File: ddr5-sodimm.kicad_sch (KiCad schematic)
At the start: 22 parts, among them J2 BUS_DDR5_SODIMM_AMPHENOL_1016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

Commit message: Connect DDR hierarchical labels. Define and connect JTAG, RGMII, TDMS, UART, and SDIO buses. Reorganize schematic blocks between sheets
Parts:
- removed J2: BUS_DDR5_SODIMM_AMPHENOL_10161033-002RHLF, sodimm-ddr5-tester-footprints:DDR5_AMPHENOL_10161033-002RHLF, symbol sodimm-ddr5-tester:BUS_DDR5_SODIMM_AMPHENOL_10161033-002RHLF
- added C127: C_1u_0402, sodimm-ddr5-tester-footprints:C_0402_1005Metric, symbol sodimm-ddr5-tester:C_1u_0402
- added D9: LED_RGY_0606_APTF1616SURKCGKSYKC, sodimm-ddr5-tester-footprints:LED_RGY_1.6x1.6mm_APTF1616, symbol sodimm-ddr5-tester:LED_RGY_0606_APTF1616SURKCGKSYKC
- added J2: Bus_DDR5_SODIMM_Amphenol_10161033-002RHLF_2xDetec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, antmicro-footprints:Bus_DDR5_SODIMM_Amphenol_10161033-002RHLF, symbol antmicroMemoryConnectorsPCCardSockets:Bus_DDR5_SODIMM_Amphenol_10161033-002RHLF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
- added Q10, Q11, Q9: BSS138PW, sodimm-ddr5-tester-footprints:SC70-3, symbol sodimm-ddr5-tester:BSS138PW
- added R128: R_10k_0402, sodimm-ddr5-tester-footprints:R_0402_1005Metric, symbol sodimm-ddr5-tester:R_10k_0402
- added R61, R62, R63: R_330R_0402, sodimm-ddr5-tester-footprints:R_0402_1005Metric, symbol sodimm-ddr5-tester:R_330R_0402
- added R78: R_4k7_0402, sodimm-ddr5-tester-footprints:R_0402_1005Metric, symbol sodimm-ddr5-tester:R_4k7_0402
- added SW3: SW_KMR211NGLFS_SMD, sodimm-ddr5-tester-footprints:SW_KMR211NGLFS_SMD, symbol sodimm-ddr5-tester:SW_KMR211NGLFS_SMD
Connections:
- net +3V3: now also D9.1 (A), R78.1
- net +5V: now also J2.1 (VIN_BULK), J2.3 (VIN_BULK)
- net A.DQ0: now also J2.11 (DQ0_A)
- net A.DQ1: now also J2.12 (DQ1_A)
- net B.DQ0: now also J2.179 (DQ0_B)
- net B.DQ1: now also J2.180 (DQ1_B)
- net Control.~{ALERT}: now also J2.108 (ALERT_n)
- net GND: now also C127.2, J2.10 (VSS), J2.101 (VSS), J2.104 (VSS), J2.105 (VSS), J2.111 (VSS), J2.112 (VSS), J2.117 (VSS), J2.118 (VSS), J2.123 (VSS), J2.129 (VSS), J2.13 (VSS), J2.135 (VSS), J2.136 (VSS), J2.14 (VSS), J2.141 (VSS), J2.142 (VSS), J2.147 (VSS), J2.148 (VSS), J2.153 (VSS), J2.154 (VSS), J2.159 (VSS), J2.160 (VSS), J2.166 (VSS), J2.167 (VSS), J2.17 (VSS), J2.170 (VSS), J2.173 (VSS), J2.174 (VSS), J2.177 (VSS), J2.178 (VSS), J2.18 (VSS), J2.181 (VSS), J2.182 (VSS), J2.185 (VSS), J2.186 (VSS), J2.189 (VSS), J2.192 (VSS), J2.193 (VSS), J2.196 (VSS), J2.197 (VSS), J2.200 (VSS), J2.201 (VSS), J2.204 (VSS), J2.205 (VSS), J2.208 (VSS), J2.21 (VSS), J2.211 (VSS), J2.212 (VSS), J2.215 (VSS), J2.216 (VSS), J2.219 (VSS), J2.220 (VSS), J2.223 (VSS), J2.224 (VSS), J2.227 (VSS), J2.228 (VSS), J2.231 (VSS), J2.234 (VSS), J2.235 (VSS), J2.238 (VSS), J2.239 (VSS), J2.24 (VSS), J2.242 (VSS), J2.243 (VSS), J2.246 (VSS), J2.247 (VSS), J2.25 (VSS), J2.250 (VSS), J2.253 (VSS), J2.254 (VSS), J2.257 (VSS), J2.258 (VSS), J2.261 (VSS), J2.262 (VSS), J2.28 (VSS), J2.29 (VSS), J2.32 (VSS), J2.33 (VSS), J2.36 (VSS), J2.37 (VSS), J2.40 (VSS), J2.43 (VSS), J2.44 (VSS), J2.47 (VSS), J2.48 (VSS), J2.51 (VSS), J2.52 (VSS), J2.55 (VSS), J2.56 (VSS), J2.59 (VSS), J2.60 (VSS), J2.63 (VSS), J2.66 (VSS), J2.67 (VSS), J2.70 (VSS), J2.71 (VSS), J2.74 (VSS), J2.75 (VSS), J2.78 (VSS), J2.79 (VSS), J2.82 (VSS), J2.85 (VSS), J2.86 (VSS), J2.89 (VSS), J2.9 (VSS), J2.90 (VSS), J2.93 (VSS), J2.94 (VSS), J2.97 (VSS), J2.98 (VSS), J2.SH, Q10.2 (S), Q11.2 (S), Q9.2 (S), R128.1, SW3.1, SW3.2
- net HSA: now also J2.2 (HSA), R128.2
- net HSCL: now also J2.4 (HSCL)
- net HSDA: now also J2.6 (HSDA)
- net RFU1: now also J2.5 (RFU)
- net RFU2: now also J2.128 (RFU)
- net RFU3: now also J2.143 (RFU)
- net VSS_DET1: now also J2.124 (VSS_DET_1)
- net VSS_DET2: now also J2.130 (VSS_DET_2)
- net at R37.1, R38.1: now also J2.8 (PWR_EN)
- net at R31.2, R36.1: now also J2.7 (PWR_GOOD)
- net PWR_EN renamed Control.PWR_EN
- net PWR_GOOD renamed Control.PWR_GOOD
- new net: D9.2 (C_{R}), R63.1
- new net: Q11.3 (D), R63.2
- new net: D9.3 (C_{G}), R62.1
- new net: Q10.3 (D), R62.2
- new net: D9.4 (C_{Y}), R61.1
- new net: Q9.3 (D), R61.2
- new net A.CA0: J2.107 (CA0_A)
- new net A.CA1: J2.109 (CA1_A)
- new net A.CA10: J2.125 (CA10_A)
- new net A.CA11: J2.126 (CA11_A)
- new net A.CA12: J2.127 (CA12_A)
- new net A.CA2: J2.113 (CA2_A)
- new net A.CA3: J2.114 (CA3_A)
- new net A.CA4: J2.115 (CA4_A)
- new net A.CA5: J2.116 (CA5_A)
- new net A.CA6: J2.119 (CA6_A)
- new net A.CA7: J2.120 (CA7_A)
- new net A.CA8: J2.121 (CA8_A)
- new net A.CA9: J2.122 (CA9_A)
- new net A.CB0: J2.95 (CB0_A)
- new net A.CB1: J2.96 (CB1_A)
- new net A.CB2: J2.99 (CB2_A)
- new net A.CB3: J2.103 (CB3_A)
- new net A.CK0_N: J2.133 (CK0_A_c)
- new net A.CK0_P: J2.131 (CK0_A_t)
- new net A.CK1_N: J2.134 (CK1_A_c)
- new net A.CK1_P: J2.132 (CK1_A_t)
- new net A.DQ10: J2.35 (DQ10_A)
- new net A.DQ11: J2.38 (DQ11_A)
- new net A.DQ12: J2.45 (DQ12_A)
- new net A.DQ13: J2.46 (DQ13_A)
- new net A.DQ14: J2.49 (DQ14_A)
- new net A.DQ15: J2.50 (DQ15_A)
- new net A.DQ16: J2.53 (DQ16_A)
- new net A.DQ17: J2.54 (DQ17_A)
- new net A.DQ18: J2.57 (DQ18_A)
- new net A.DQ19: J2.58 (DQ19_A)
- new net A.DQ2: J2.15 (DQ2_A)
- new net A.DQ20: J2.65 (DQ20_A)
- new net A.DQ21: J2.68 (DQ21_A)
- new net A.DQ22: J2.69 (DQ22_A)
- new net A.DQ23: J2.72 (DQ23_A)
- new net A.DQ24: J2.73 (DQ24_A)
- new net A.DQ25: J2.76 (DQ25_A)
- new net A.DQ26: J2.77 (DQ26_A)
- new net A.DQ27: J2.80 (DQ27_A)
- new net A.DQ28: J2.87 (DQ28_A)
- new net A.DQ29: J2.88 (DQ29_A)
- new net A.DQ3: J2.16 (DQ3_A)
- new net A.DQ30: J2.91 (DQ30_A)
- new net A.DQ31: J2.92 (DQ31_A)
- new net A.DQ4: J2.23 (DQ4_A)
- new net A.DQ5: J2.26 (DQ5_A)
- new net A.DQ6: J2.27 (DQ6_A)
- new net A.DQ7: J2.30 (DQ7_A)
- new net A.DQ8: J2.31 (DQ8_A)
- new net A.DQ9: J2.34 (DQ09_A)
- new net A.DQS0_N: J2.20 (DQS0_A_C)
- new net A.DQS0_P: J2.22 (DQS0_A_t)
- new net A.DQS1_N: J2.39 (DQS1_A_C)
- new net A.DQS1_P: J2.41 (DQS1_A_t)
- new net A.DQS2_N: J2.62 (DQS2_A_C)
- new net A.DQS2_P: J2.64 (DQS2_A_t)
- new net A.DQS3_N: J2.81 (DQS3_A_C)
- new net A.DQS3_P: J2.83 (DQS3_A_t)
- new net A.DQS4_N: J2.100 (DQS4_A_c)
- new net A.DQS4_P: J2.102 (DQS4_A_t)
- new net A.~{CS0}: J2.106 (CS0_A_n)
- new net A.~{CS1}: J2.110 (CS1_A_n)
- new net A.~{DM0}: J2.19 (DM0_A_n)
- new net A.~{DM1}: J2.42 (DM1_A_n)
- new net A.~{DM2}: J2.61 (DM2_A_n)
- new net A.~{DM3}: J2.84 (DM3_A_n)
- new net B.CA0: J2.164 (CA0_B)
- new net B.CA1: J2.162 (CA1_B)
- new net B.CA10: J2.146 (CA10_B)
- new net B.CA11: J2.145 (CA11_B)
- new net B.CA12: J2.144 (CA12_B)
- new net B.CA2: J2.158 (CA2_B)
- new net B.CA3: J2.157 (CA3_B)
- new net B.CA4: J2.156 (CA4_B)
- new net B.CA5: J2.155 (CA5_B)
- new net B.CA6: J2.152 (CA6_B)
- new net B.CA7: J2.151 (CA7_B)
- new net B.CA8: J2.150 (CA8_B)
- new net B.CA9: J2.149 (CA9_B)
- new net B.CB0: J2.168 (CB0_B)
- new net B.CB1: J2.172 (CB1_B)
- new net B.CB2: J2.176 (CB2_B)
- new net B.CB3: J2.175 (CB3_B)
- new net B.CK0_N: J2.139 (CK0_B_c)
- new net B.CK0_P: J2.137 (CK0_B_t)
- new net B.CK1_N: J2.140 (CK1_B_C)
- new net B.CK1_P: J2.138 (CK1_B_t)
- new net B.DQ10: J2.203 (DQ10_B)
- new net B.DQ11: J2.206 (DQ11_B)
- new net B.DQ12: J2.213 (DQ12_B)
- new net B.DQ13: J2.214 (DQ13_B)
- new net B.DQ14: J2.217 (DQ14_B)
- new net B.DQ15: J2.218 (DQ15_B)
- new net B.DQ16: J2.221 (DQ16_B)
- new net B.DQ17: J2.222 (DQ17_B)
- new net B.DQ18: J2.225 (DQ18_B)
- new net B.DQ19: J2.226 (DQ19_B)
- new net B.DQ2: J2.183 (DQ2_B)
- new net B.DQ20: J2.233 (DQ20_B)
- new net B.DQ21: J2.236 (DQ21_B)
- new net B.DQ22: J2.237 (DQ22_B)
- new net B.DQ23: J2.240 (DQ23_B)
- new net B.DQ24: J2.241 (DQ24_B)
- new net B.DQ25: J2.244 (DQ25_B)
- new net B.DQ26: J2.245 (DQ26_B)
- new net B.DQ27: J2.248 (DQ27_B)
- new net B.DQ28: J2.255 (DQ28_B)
- new net B.DQ29: J2.256 (DQ29_B)
- new net B.DQ3: J2.184 (DQ3_B)
- new net B.DQ30: J2.259 (DQ30_B)
- new net B.DQ31: J2.260 (DQ31_B)
- new net B.DQ4: J2.191 (DQ4_B)
- new net B.DQ5: J2.194 (DQ5_B)
- new net B.DQ6: J2.195 (DQ6_B)
- new net B.DQ7: J2.198 (DQ7_B)
- new net B.DQ8: J2.199 (DQ8_B)
- new net B.DQ9: J2.202 (DQ9_B)
- new net B.DQS0_N: J2.188 (DQS0_B_C)
- new net B.DQS0_P: J2.190 (DQS0_B_t)
- new net B.DQS1_N: J2.207 (DQS1_B_C)
- new net B.DQS1_P: J2.209 (DQS1_B_t)
- new net B.DQS2_N: J2.230 (DQS2_B_C)
- new net B.DQS2_P: J2.232 (DQS2_B_t)
- new net B.DQS3_N: J2.249 (DQS3_B_c)
- new net B.DQS3_P: J2.251 (DQS3_B_t)
- new net B.DQS4_N: J2.169 (DQS4_B_c)
- new net B.DQS4_P: J2.171 (DQS4_B_T)
- new net B.~{CS0}: J2.161 (CS0_B_n)
- new net B.~{CS1}: J2.165 (CS1_B_N)
- new net B.~{DM0}: J2.187 (DM0_B_n)
- new net B.~{DM1}: J2.210 (DM1_B_n)
- new net B.~{DM2}: J2.229 (DM2_B_n)
- new net B.~{DM3}: J2.252 (DM3_B_n)
- new net Control.~{RESET}: J2.163 (RESET_n)
- new net HOT_SWAP_BUTTON: C127.1, R78.2, SW3.3, SW3.4
- new net HOT_SWAP_GREEN: Q10.1 (G)
- new net HOT_SWAP_RED: Q11.1 (G)
- new net HOT_SWAP_YELLOW: Q9.1 (G)
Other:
- note added: "Default 000"
- note added: "HOT SWAP eject button"
- note added: "HOT SWAP status LED"
- note added: "Optional RC filter, tr=10ms"
- note added: "Serial adress select"
- note removed: "..."
- moved on the sheet: C6, C7, R31, R36, R37, R38

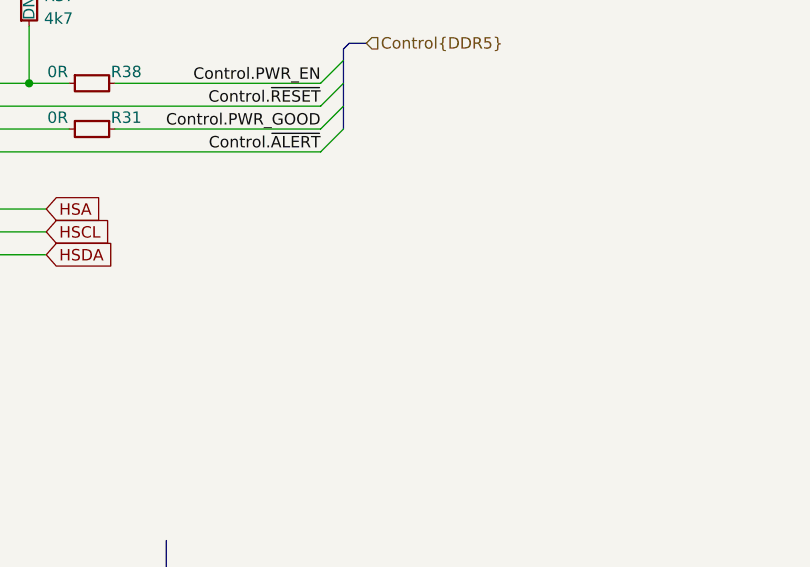
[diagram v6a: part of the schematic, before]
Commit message: Finish creating hierarchical buses and structure, start reconnecting signals
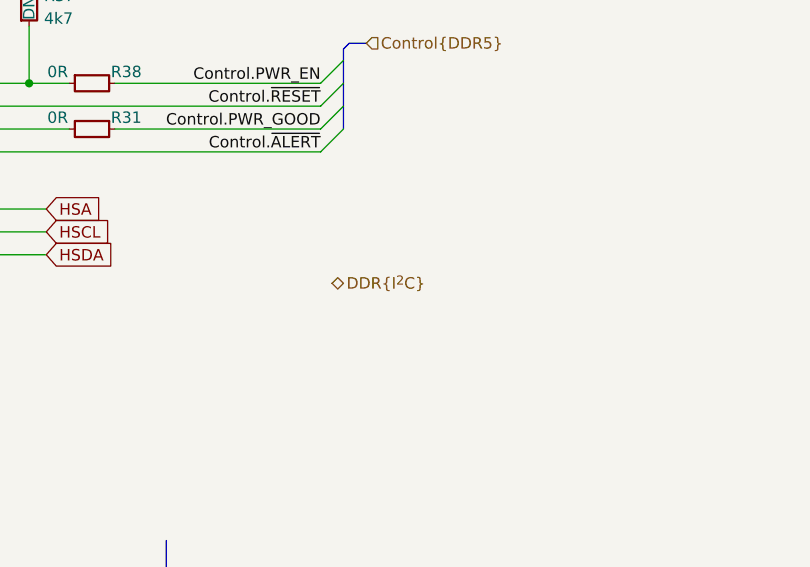
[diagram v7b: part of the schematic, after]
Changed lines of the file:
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@@
     )
+  )
+  (hierarchical_label "DDR{I^{2}C}" (shape bidirectional) (at 358.14 105.41 0)
+    (effects (font (size 1.27 1.27)) (justify left))
   )
   (hierarchical_label "B{DDR5}" (shape input) (at 219.075 67.945 0)

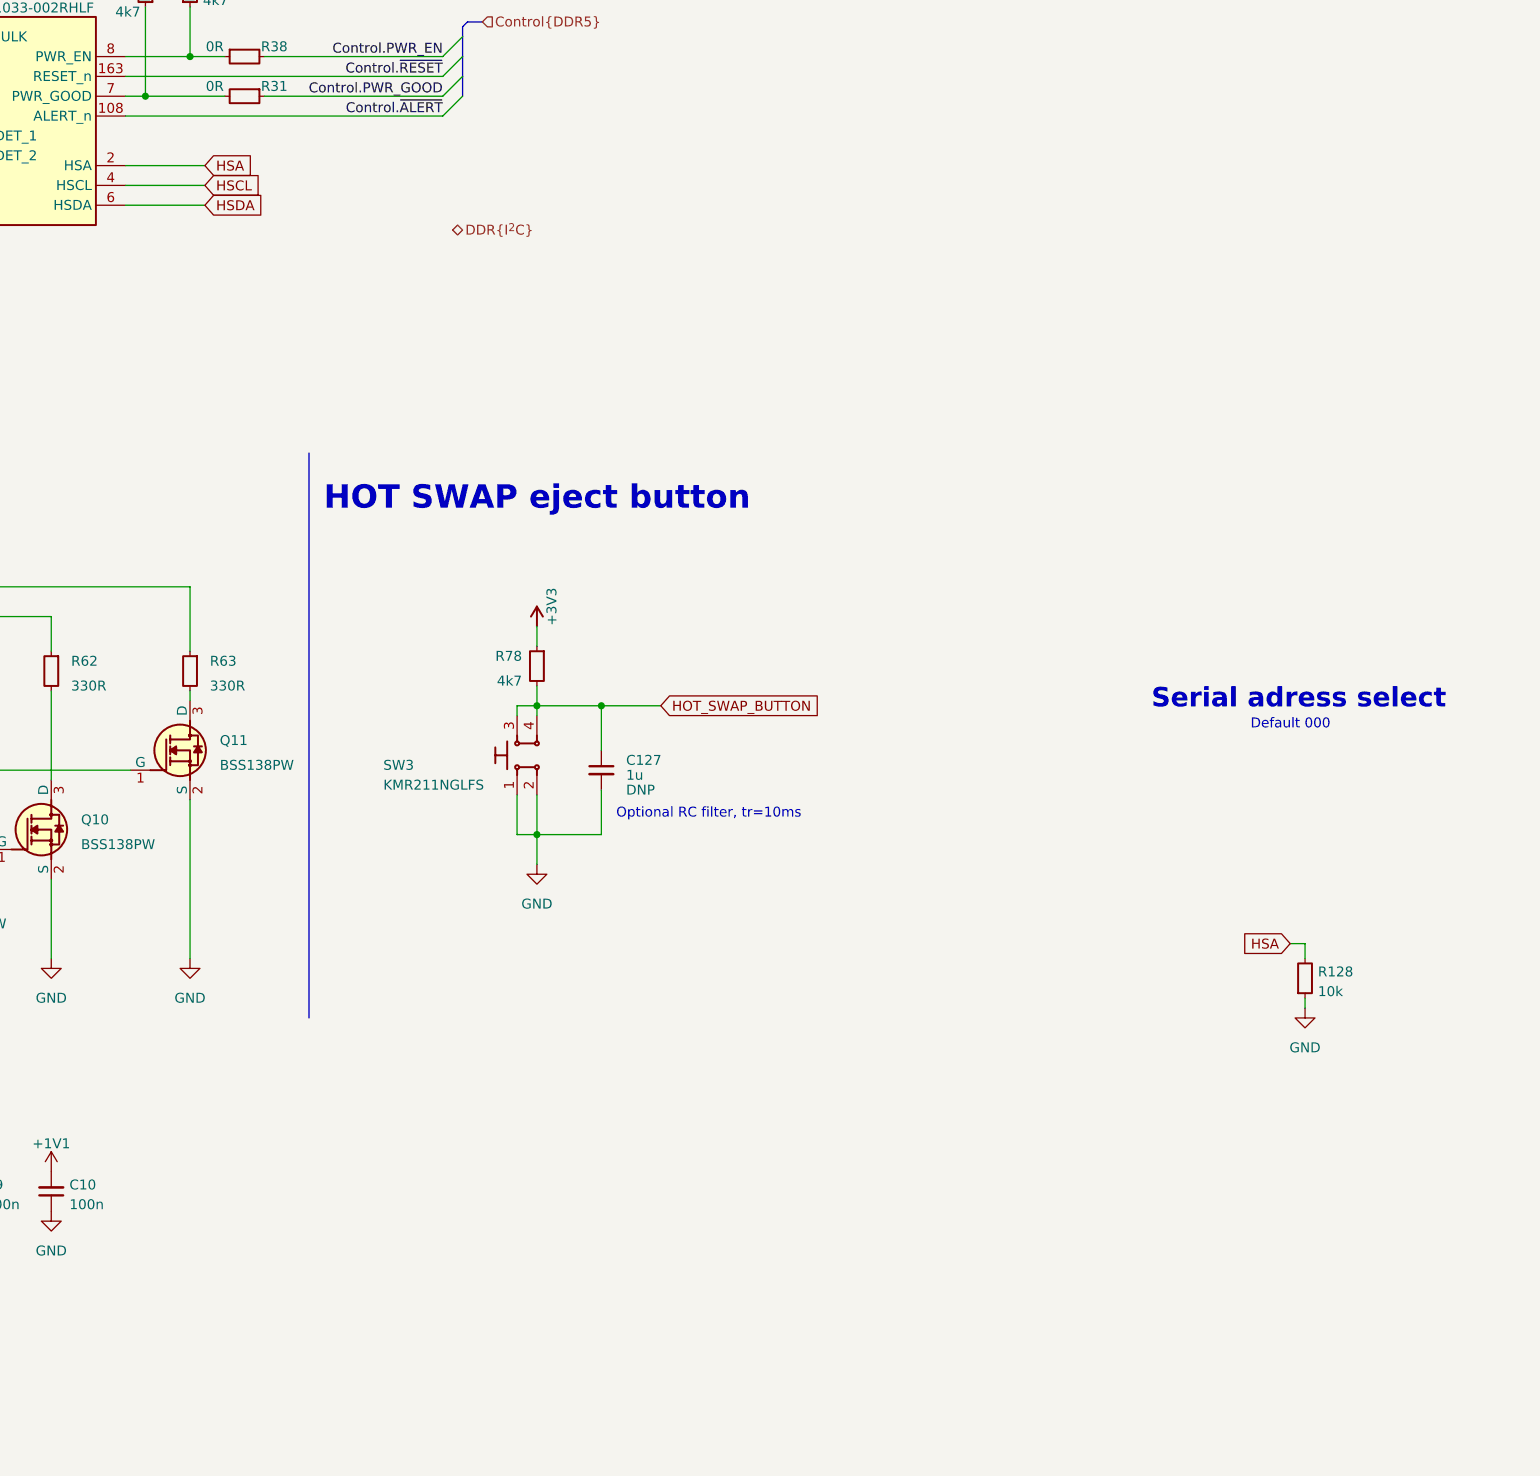
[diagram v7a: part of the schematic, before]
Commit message: Finish reconnecting signals after migration to the hierarchical structure
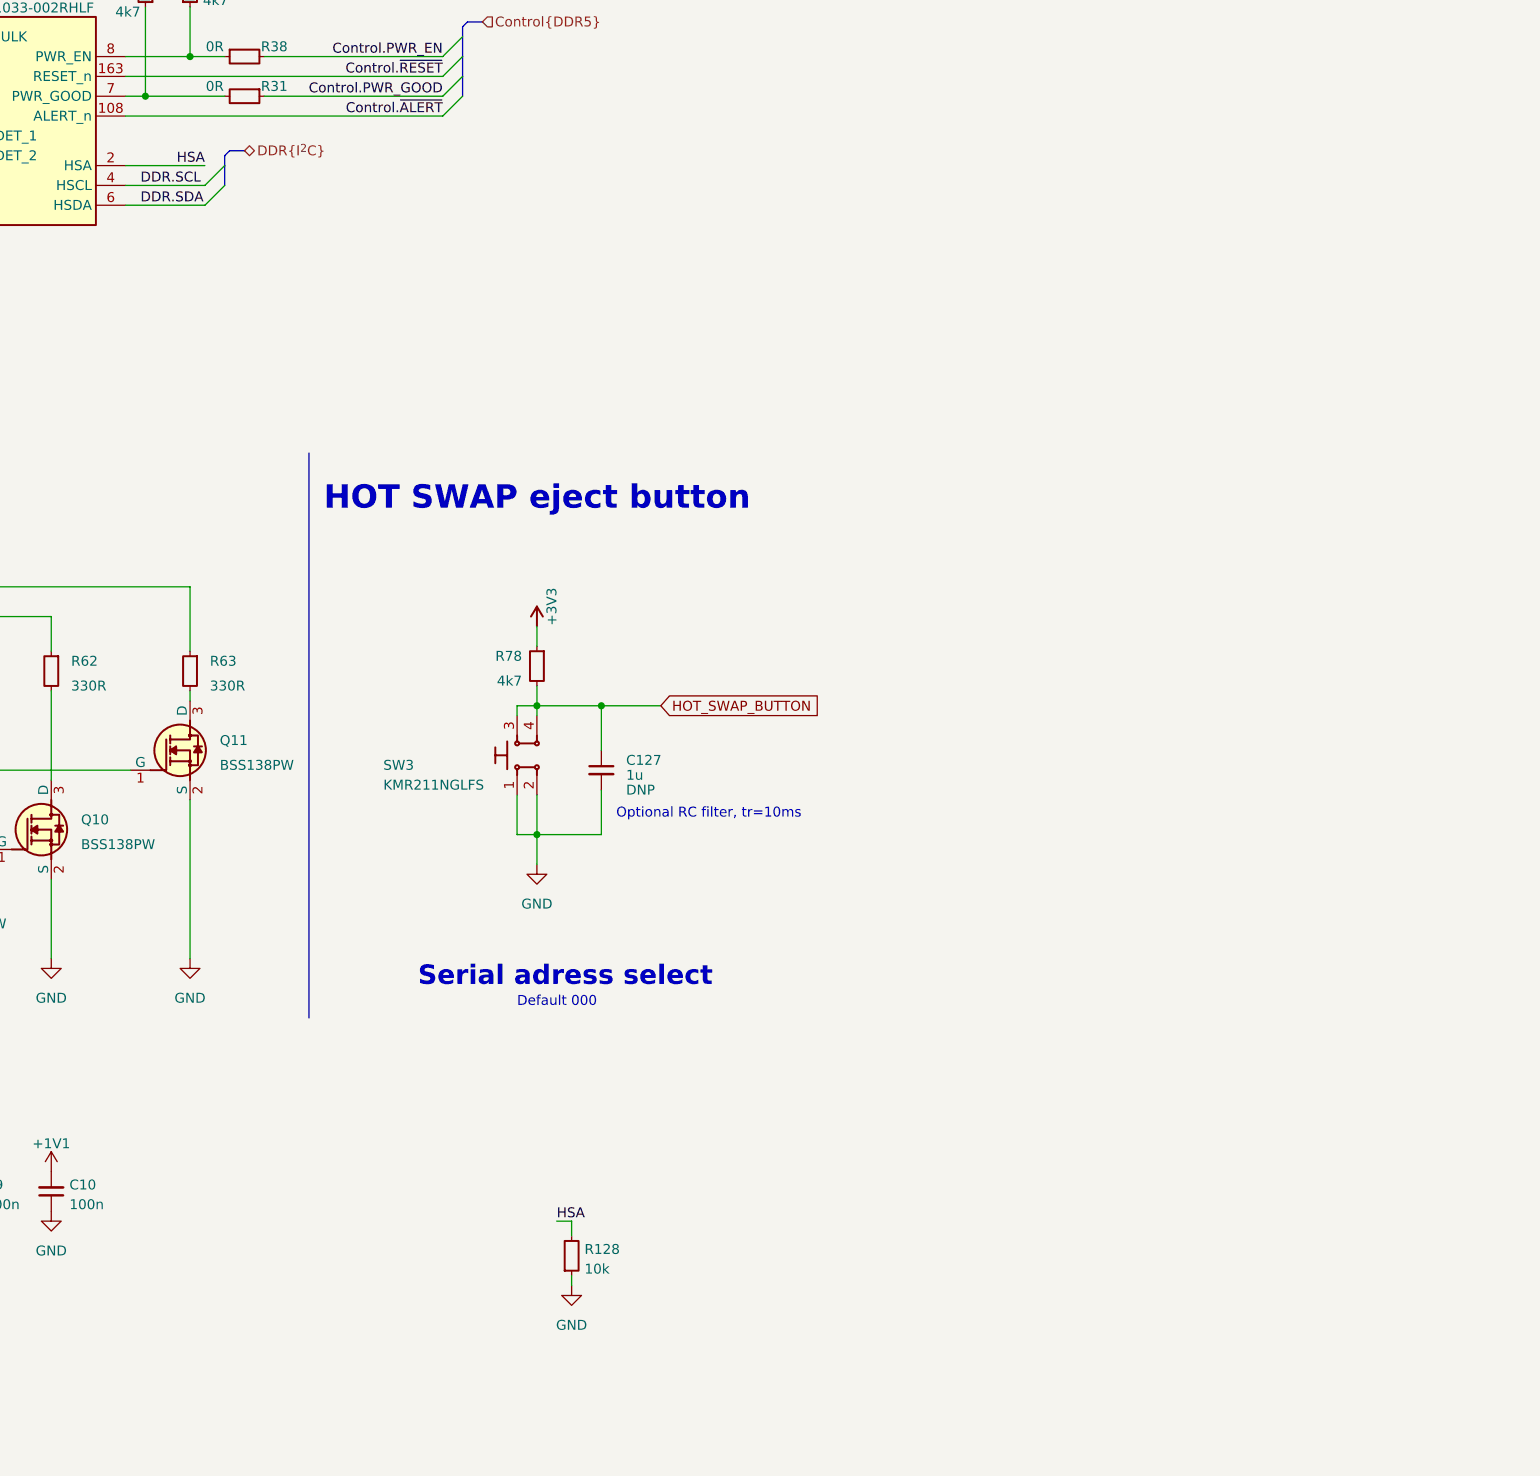
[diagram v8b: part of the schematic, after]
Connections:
- net HSCL renamed DDR.SCL
- net HSDA renamed DDR.SDA
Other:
- moved on the sheet: R128
